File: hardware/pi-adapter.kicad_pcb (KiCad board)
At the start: 2 copper layers, 64 x 56 mm, 37 parts, among them P1 CONN_01X04, P10 CONN_01X04, P11 CONN_01X04, P12 CONN_01X04, P13 CONN_01X04, P14 CONN_01X04, P15 CONN_01X04, P16 CONN_01X04, P2 CONN_01X04, P20 CONN_02X20, P21 CONN_01X03, P22 CONN_01X06, P23 CONN_01X03, P3 CONN_01X04, P30 +5V, P31 GND, P4 CONN_01X04, P40 CONN_01X01, P41 CONN_01X01, P43 CONN_01X01, P5 CONN_01X04, P6 CONN_01X04, P7 CONN_01X04, P8 CONN_01X04, P9 CONN_01X04, U1 74HCT245, U2 74HCT245, U3 74HCT245, U4 74HCT245

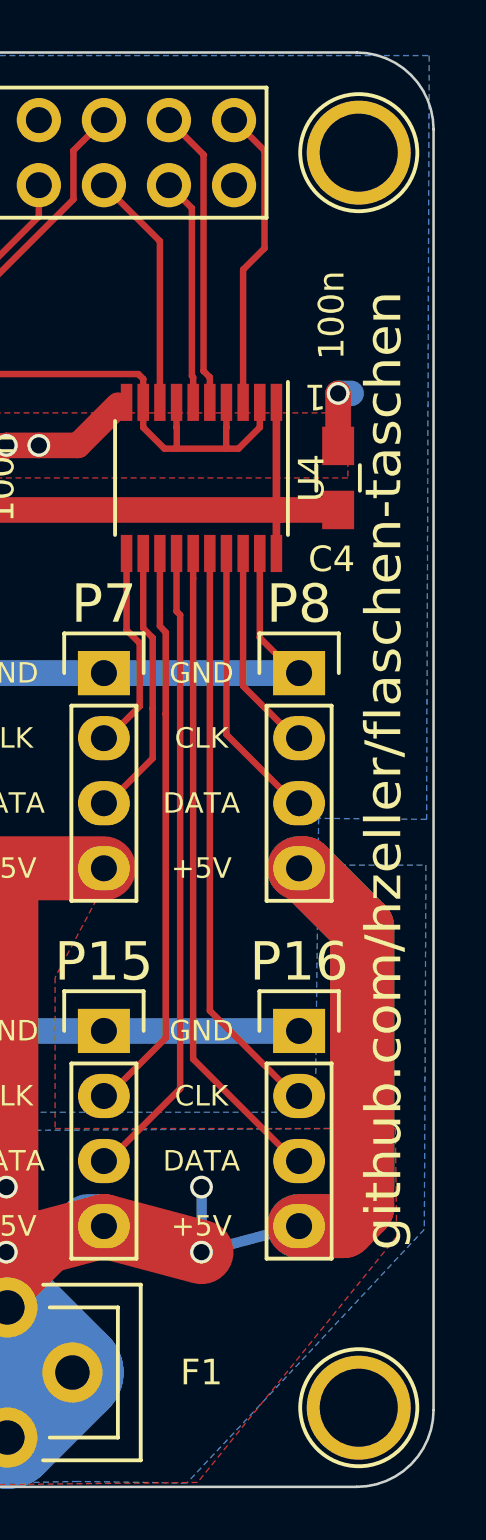
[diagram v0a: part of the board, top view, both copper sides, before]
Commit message: Update silk-screen text to point to spixels github.
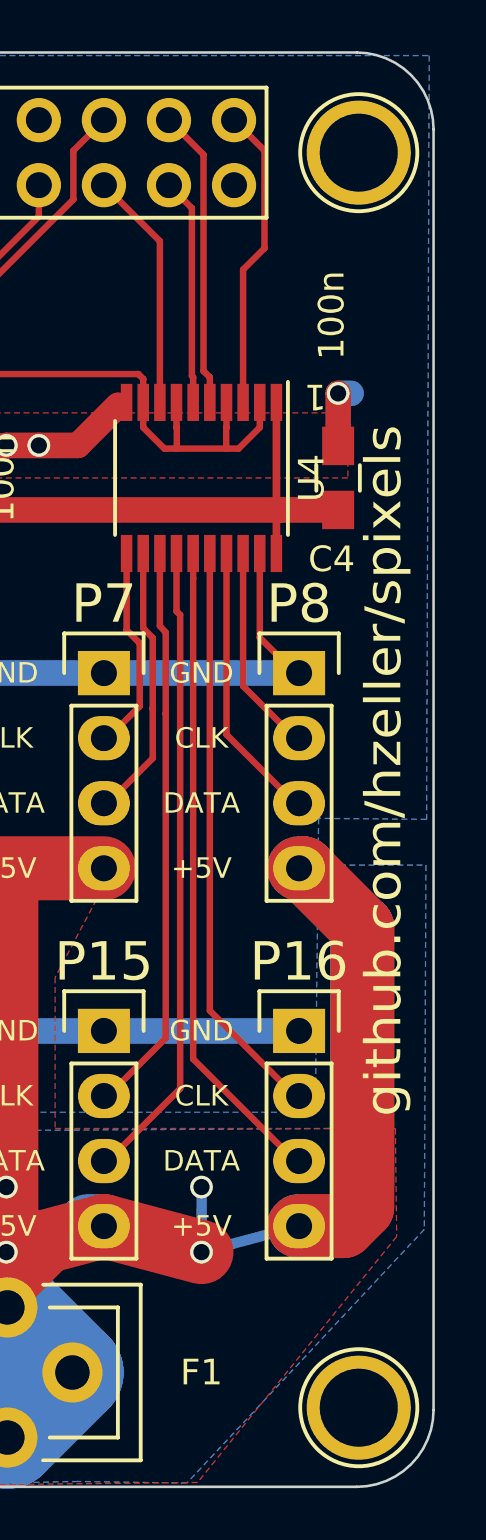
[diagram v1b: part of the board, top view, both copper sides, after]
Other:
- board text added: "github.com/hzeller/spixels"
- board text removed: "github.com/hzeller/flaschen-taschen"
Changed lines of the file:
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@@
-(kicad_pcb (version 4) (host pcbnew "(2015-08-05 BZR 6054, Git 5c8efeb)-product")
+(kicad_pcb (version 20170123) (host pcbnew "(2017-03-23 revision f2763e90e)-master")
   (general
     (links 150)
     (no_connects 0)
-    (area 97.971667 37.949999 166.188334 96.86)
+    (area 97.971667 37.949999 166.188334 96.9775)
     (thickness 1.6)
     (drawings 84)
@@
       (hpglpenspeed 20)
       (hpglpendiameter 15)
-      (hpglpenoverlay 2)
       (psnegative false)
       (psa4output false)
@@
       (effects (font (size 1 1) (thickness 0.15)) (justify mirror))
     )
-    (fp_text value Symbol_OSHW-Logo_SilkScreen (at 5.461 -5.461 450) (layer B.Fab) hide
+    (fp_text value Symbol_OSHW-Logo_SilkScreen (at 5.461 -5.461 90) (layer B.Fab) hide
       (effects (font (size 1 1) (thickness 0.15)) (justify mirror))
     )
@@
     (effects (font (size 1 1) (thickness 0.25)))
   )
-  (gr_text github.com/hzeller/flaschen-taschen (at 162.052 66.04 90) (layer F.SilkS)
+  (gr_text github.com/hzeller/spixels (at 162.052 66.04 90) (layer F.SilkS)
     (effects (font (size 1.4 1.5) (thickness 0.2)))
   )
